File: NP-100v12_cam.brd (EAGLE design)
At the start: 170 x 104 mm, 100 parts, among them IC1 LM317, IC2 LM317, IC3 LM317T, IC4 7805TV, IC5 7805TV, IC6 7812L, K1 351, Q1 2N3904, Q2 2N3904, Q3 IRF510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

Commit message: - Added resistor between the wiper and ground of the volume pot
 - Added missing ground connection to the volume pot
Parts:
- added R22, R23: 1M, adafruit:0207/10
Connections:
- net N$32: now also R22.1, R23.1, VOLUME.G1, VOLUME.G2
- net N$34: now also R23.2
- net N$35: now also R22.2
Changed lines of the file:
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@@
 </element>
 <element name="IC4" library="linear" package="TO220V" value="7805TV" x="73.9775" y="0.635" rot="R180"/>
+<element name="R22" library="adafruit" package="0207/10" value="1M" x="179.07" y="85.09" rot="R90"/>
+<element name="R23" library="adafruit" package="0207/10" value="1M" x="179.07" y="72.39" rot="R270"/>
 </elements>
 <signals>
@@
 <wire x1="158.75" y1="101.6" x2="160.02" y2="100.33" width="1.27" layer="16"/>
 <wire x1="160.02" y1="100.33" x2="160.02" y2="95.885" width="1.27" layer="16"/>
+<contactref element="VOLUME" pad="G2"/>
+<contactref element="VOLUME" pad="G1"/>
+<contactref element="R22" pad="1"/>
+<contactref element="R23" pad="1"/>
+<wire x1="157.06" y1="73.74" x2="167.06" y2="73.74" width="0" layer="19" extent="1-1"/>
+<wire x1="160.02" y1="95.885" x2="157.06" y2="73.74" width="0" layer="19" extent="1-1"/>
+<wire x1="179.07" y1="80.01" x2="157.06" y2="73.74" width="0" layer="19" extent="1-1"/>
+<wire x1="179.07" y1="77.47" x2="179.07" y2="80.01" width="0" layer="19" extent="1-1"/>
 </signal>
 <signal name="N$33">
@@
 <wire x1="149.225" y1="81.915" x2="152.4" y2="78.74" width="1.27" layer="16"/>
 <wire x1="152.4" y1="78.74" x2="157.06" y2="78.74" width="1.27" layer="16"/>
+<contactref element="R23" pad="2"/>
+<wire x1="179.07" y1="67.31" x2="149.225" y2="81.915" width="0" layer="19" extent="16-16"/>
 </signal>
 <signal name="N$35">
@@
 <wire x1="155.8925" y1="81.28" x2="164.52" y2="81.28" width="1.27" layer="16"/>
 <wire x1="164.52" y1="81.28" x2="167.06" y2="78.74" width="1.27" layer="16"/>
+<contactref element="R22" pad="2"/>
+<wire x1="179.07" y1="90.17" x2="154.305" y2="83.185" width="0" layer="19" extent="16-16"/>
 </signal>
 <signal name="N$36">

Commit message: - Added code for the turn on delay
 - Added arduino/visual micro/visual studio specific info to the gitignore file
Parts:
- moved R23 29.0 mm to (152.4, 61.0), turned to 180 degrees
- moved R22 26.4 mm to (163.8, 63.5), turned to 180 degrees
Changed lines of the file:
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@@
 </element>
 <element name="IC4" library="linear" package="TO220V" value="7805TV" x="73.9775" y="0.635" rot="R180"/>
-<element name="R22" library="adafruit" package="0207/10" value="1M" x="179.07" y="85.09" rot="R90"/>
-<element name="R23" library="adafruit" package="0207/10" value="1M" x="179.07" y="72.39" rot="R270"/>
+<element name="R22" library="adafruit" package="0207/10" value="1M" x="163.83" y="63.5" rot="R180"/>
+<element name="R23" library="adafruit" package="0207/10" value="1M" x="152.4" y="60.96" rot="R180"/>
 </elements>
 <signals>
@@
 <wire x1="96.139" y1="8.1915" x2="96.139" y2="3.2004" width="1.27" layer="16"/>
 <contactref element="IC4" pad="2"/>
+<wire x1="73.9775" y1="3.175" x2="73.9775" y2="18.7325" width="0.6096" layer="1"/>
+<wire x1="73.9775" y1="18.7325" x2="67.31" y2="25.4" width="0.6096" layer="1"/>
 <wire x1="91.186" y1="100.9396" x2="78.4225" y2="101.6" width="0" layer="19" extent="16-16"/>
 <wire x1="80.01" y1="49.53" x2="83.82" y2="53.34" width="0" layer="19" extent="16-16"/>
+<wire x1="67.31" y1="25.4" x2="68.58" y2="26.67" width="0" layer="19" extent="1-16"/>
 <wire x1="64.77" y1="30.48" x2="67.31" y2="27.94" width="0" layer="19" extent="16-16"/>
 <wire x1="59.69" y1="28.8925" x2="59.69" y2="31.75" width="0" layer="19" extent="16-16"/>
 <wire x1="40.767" y1="20.8026" x2="40.64" y2="20.32" width="0" layer="19" extent="16-16"/>
-<wire x1="73.9775" y1="3.175" x2="73.9775" y2="18.7325" width="0.6096" layer="1"/>
-<wire x1="73.9775" y1="18.7325" x2="67.31" y2="25.4" width="0.6096" layer="1"/>
-<wire x1="67.31" y1="25.4" x2="68.58" y2="26.67" width="0" layer="19" extent="1-16"/>
 </signal>
 <signal name="N$2">
@@
 <via x="18.7325" y="22.225" extent="1-16" drill="1.2" diameter="2.54"/>
 <contactref element="IC4" pad="1"/>
-<wire x1="67.31" y1="34.29" x2="105.41" y2="57.2874" width="0" layer="19" extent="16-16"/>
-<wire x1="44.45" y1="30.0482" x2="59.69" y2="34.29" width="0" layer="19" extent="16-16"/>
 <wire x1="76.5175" y1="3.175" x2="76.5175" y2="20.0025" width="0.6096" layer="1"/>
 <wire x1="76.5175" y1="20.0025" x2="67.31" y2="29.21" width="0.6096" layer="1"/>
 <wire x1="67.31" y1="29.21" x2="67.31" y2="30.48" width="0.6096" layer="1"/>
+<wire x1="67.31" y1="34.29" x2="105.41" y2="57.2874" width="0" layer="19" extent="16-16"/>
 <wire x1="67.31" y1="30.48" x2="67.31" y2="32.385" width="0" layer="19" extent="1-16"/>
+<wire x1="44.45" y1="30.0482" x2="59.69" y2="34.29" width="0" layer="19" extent="16-16"/>
 </signal>
 <signal name="N$22">
@@
 <contactref element="R22" pad="1"/>
 <contactref element="R23" pad="1"/>
+<wire x1="167.06" y1="73.74" x2="168.91" y2="63.5" width="0" layer="19" extent="1-1"/>
 <wire x1="157.06" y1="73.74" x2="167.06" y2="73.74" width="0" layer="19" extent="1-1"/>
+<wire x1="157.48" y1="60.96" x2="157.06" y2="73.74" width="0" layer="19" extent="1-1"/>
 <wire x1="160.02" y1="95.885" x2="157.06" y2="73.74" width="0" layer="19" extent="1-1"/>
-<wire x1="179.07" y1="80.01" x2="157.06" y2="73.74" width="0" layer="19" extent="1-1"/>
-<wire x1="179.07" y1="77.47" x2="179.07" y2="80.01" width="0" layer="19" extent="1-1"/>
 </signal>
 <signal name="N$33">
@@
 <wire x1="152.4" y1="78.74" x2="157.06" y2="78.74" width="1.27" layer="16"/>
 <contactref element="R23" pad="2"/>
-<wire x1="179.07" y1="67.31" x2="149.225" y2="81.915" width="0" layer="19" extent="16-16"/>
+<wire x1="147.32" y1="60.96" x2="157.06" y2="78.74" width="0" layer="19" extent="1-1"/>
 </signal>
 <signal name="N$35">
@@
 <wire x1="164.52" y1="81.28" x2="167.06" y2="78.74" width="1.27" layer="16"/>
 <contactref element="R22" pad="2"/>
-<wire x1="179.07" y1="90.17" x2="154.305" y2="83.185" width="0" layer="19" extent="16-16"/>
+<wire x1="158.75" y1="63.5" x2="167.06" y2="78.74" width="0" layer="19" extent="1-1"/>
 </signal>
 <signal name="N$36">
@@
 <wire x1="60.325" y1="38.1" x2="59.69" y2="38.735" width="0.6096" layer="16"/>
 <contactref element="IC4" pad="3"/>
-<wire x1="71.12" y1="30.48" x2="73.66" y2="29.21" width="0" layer="19" extent="16-16"/>
 <wire x1="71.4375" y1="3.175" x2="71.4375" y2="28.2575" width="0.6096" layer="1"/>
 <wire x1="71.4375" y1="28.2575" x2="72.39" y2="29.21" width="0.6096" layer="1"/>
 <wire x1="72.39" y1="29.21" x2="73.66" y2="29.21" width="0" layer="19" extent="1-16"/>
+<wire x1="71.12" y1="30.48" x2="72.39" y2="29.21" width="0" layer="19" extent="1-16"/>
 </signal>
 <signal name="N$43">

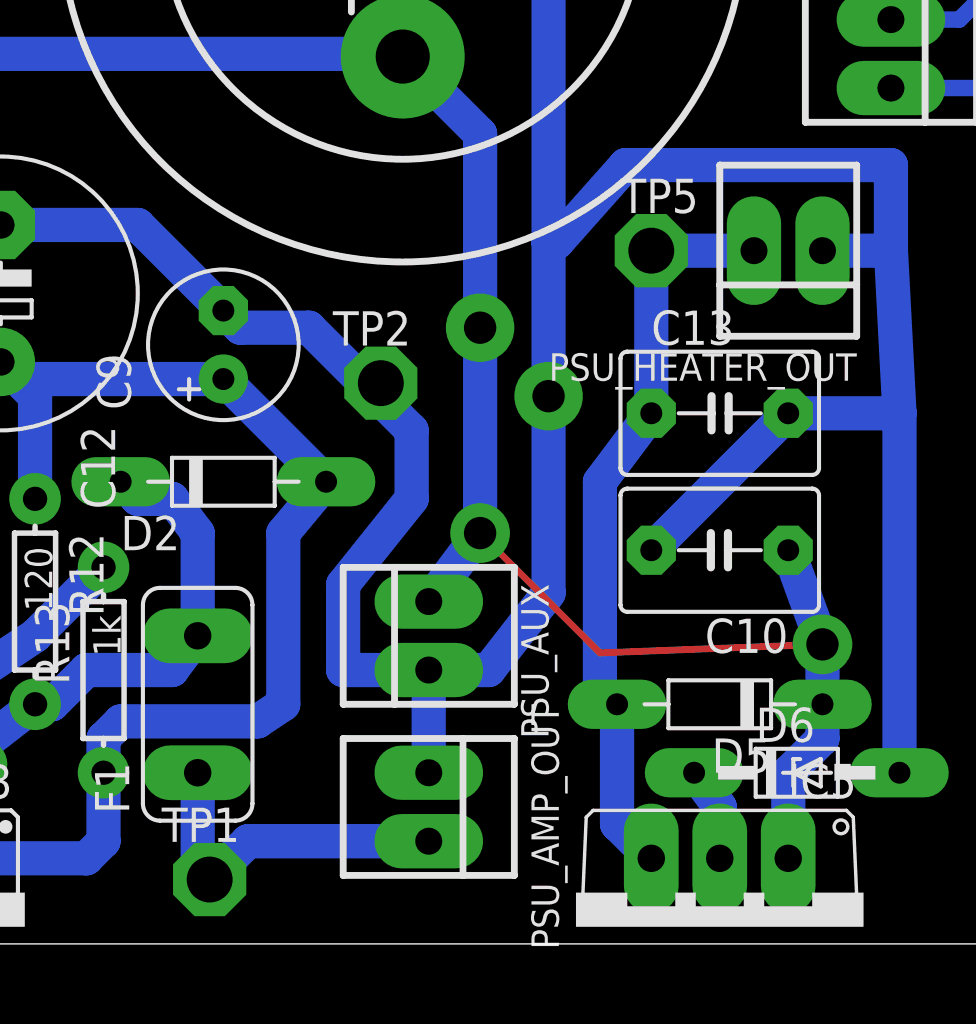
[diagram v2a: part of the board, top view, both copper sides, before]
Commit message: - Renamed the test points to reflect their function
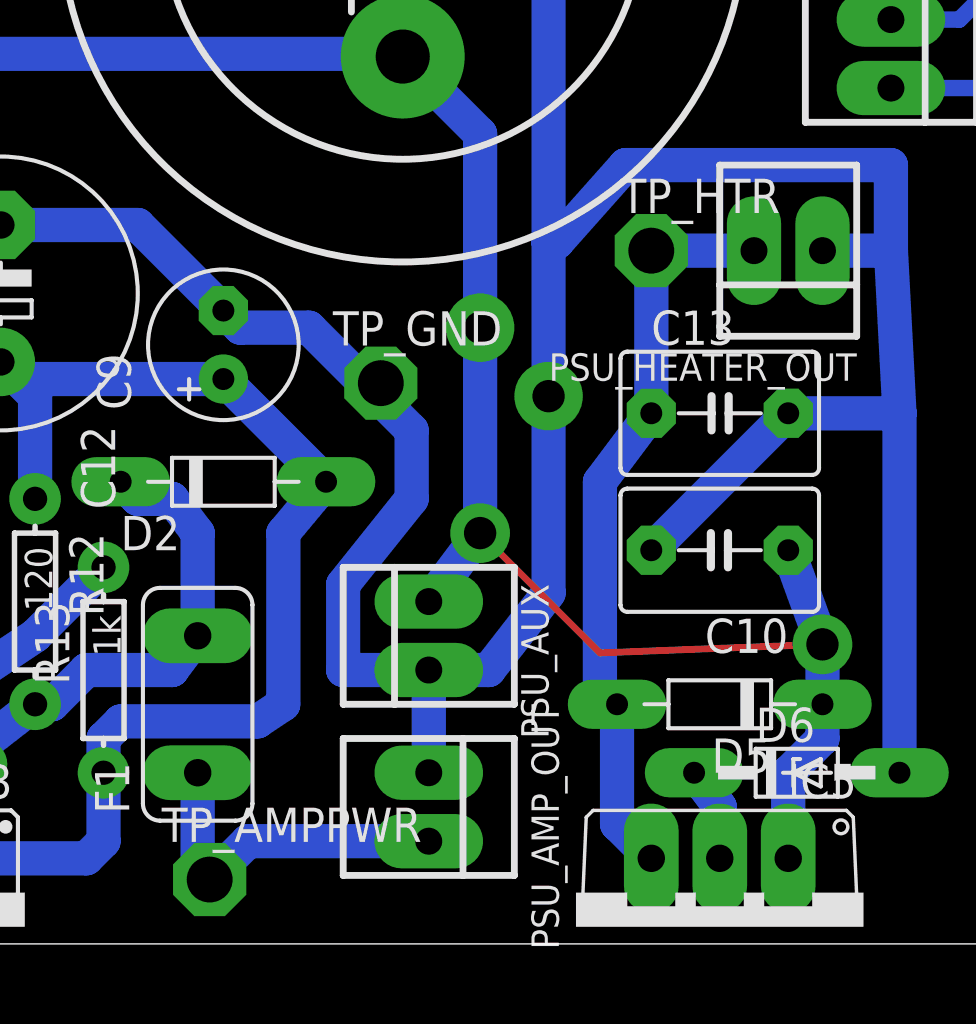
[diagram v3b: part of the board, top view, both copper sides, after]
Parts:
- renumbered TP1 to TP_AMPPWR, TP2 to TP_GND, TP5 to TP_HTR
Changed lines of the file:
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@@
 <attribute name="TP_SIGNAL_NAME" value="" x="100.9904" y="4.826" size="1.778" layer="27" rot="R180" display="off"/>
 </element>
-<element name="TP1" library="testpad" package="P1-17" value="TPPAD1-17" x="34.417" y="2.3876" smashed="yes">
+<element name="TP_AMPPWR" library="testpad" package="P1-17" value="TPPAD1-17" x="34.417" y="2.3876" smashed="yes">
 <attribute name="TP_SIGNAL_NAME" value="" x="33.147" y="-0.7874" size="1" layer="37"/>
 <attribute name="NAME" x="32.639" y="3.7846" size="1.27" layer="25" ratio="10"/>
 <attribute name="VALUE" x="34.417" y="2.3876" size="0.0254" layer="27"/>
 </element>
-<element name="TP2" library="testpad" package="P1-17" value="TPPAD1-17" x="40.767" y="20.8026" smashed="yes">
+<element name="TP_GND" library="testpad" package="P1-17" value="TPPAD1-17" x="40.767" y="20.8026" smashed="yes">
 <attribute name="TP_SIGNAL_NAME" value="" x="39.497" y="17.6276" size="1" layer="37"/>
 <attribute name="NAME" x="38.989" y="22.1996" size="1.27" layer="25" ratio="10"/>
@@
 <attribute name="OC_FARNELL" value="1462926" x="5.08" y="21.59" size="1.778" layer="27" rot="R90" display="off"/>
 </element>
-<element name="TP5" library="testpad" package="P1-17" value="TPPAD1-17" x="50.8" y="25.7175">
+<element name="TP_HTR" library="testpad" package="P1-17" value="TPPAD1-17" x="50.8" y="25.7175">
 <attribute name="TP_SIGNAL_NAME" value="" x="50.8" y="25.7175" size="1.778" layer="27" display="off"/>
 </element>
@@
 <contactref element="C9" pad="-"/>
 <contactref element="J2" pad="1"/>
-<contactref element="TP2" pad="TP"/>
+<contactref element="TP_GND" pad="TP"/>
 <contactref element="PSU_AUX" pad="1"/>
 <contactref element="POWER" pad="2"/>
@@
 <signal name="N$16">
 <contactref element="F1" pad="2"/>
-<contactref element="TP1" pad="TP"/>
+<contactref element="TP_AMPPWR" pad="TP"/>
 <wire x1="35.8394" y1="3.81" x2="34.417" y2="2.3876" width="1.27" layer="16"/>
 <wire x1="33.9725" y1="6.35" x2="33.9725" y2="2.5146" width="1.27" layer="16"/>
@@
 <wire x1="48.895" y1="9.525" x2="49.53" y2="8.89" width="1.27" layer="16"/>
 <contactref element="PSU_HEATER_OUT" pad="2"/>
-<contactref element="TP5" pad="TP"/>
+<contactref element="TP_HTR" pad="TP"/>
 <wire x1="50.8" y1="25.7175" x2="50.8" y2="19.685" width="1.27" layer="16"/>
 <wire x1="50.8" y1="25.7175" x2="54.61" y2="25.7175" width="1.27" layer="16"/>
